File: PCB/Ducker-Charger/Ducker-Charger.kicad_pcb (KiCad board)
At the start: 2 copper layers, 7 parts, among them J1 Conn_01x02, Q1 NCE3080K, Q2 NCE3080K, Q3 NCE3080K, Q4 NCE3080K, U1 IP5389_CN_AACD_WC4QD

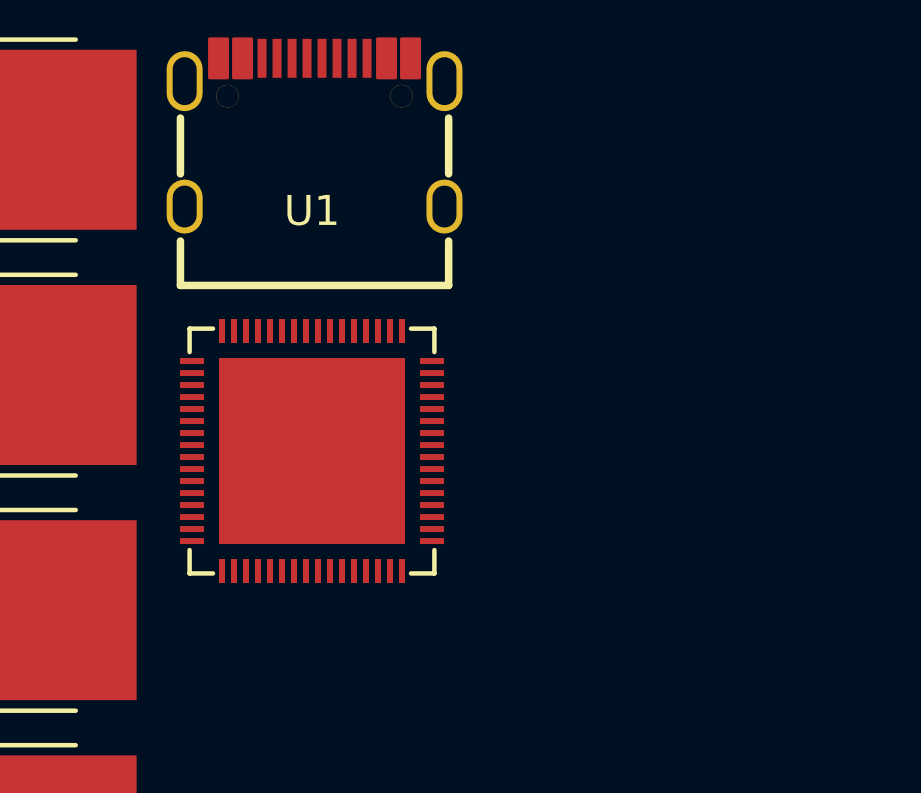
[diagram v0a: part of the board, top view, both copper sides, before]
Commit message: feat: started BMS configuration
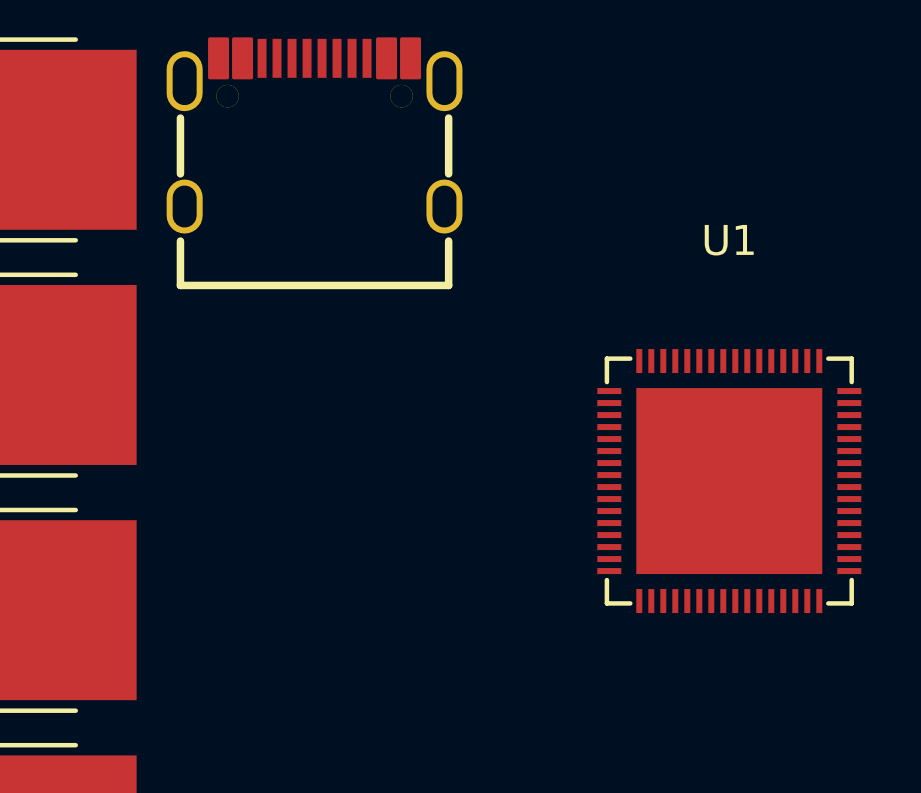
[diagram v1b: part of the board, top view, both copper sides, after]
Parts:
- moved U1 13.9 mm to (270.2, 140.2)
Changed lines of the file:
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@@
 	(footprint "EasyEDA:QFN-64_L8.0-W8.0-P0.40-TL-EP6.2"
 		(layer "F.Cu")
-		(at 256.32 139.16)
+		(at 270.23 140.16)
 		(property "Reference" "U1"
 			(at 0 -8 0)

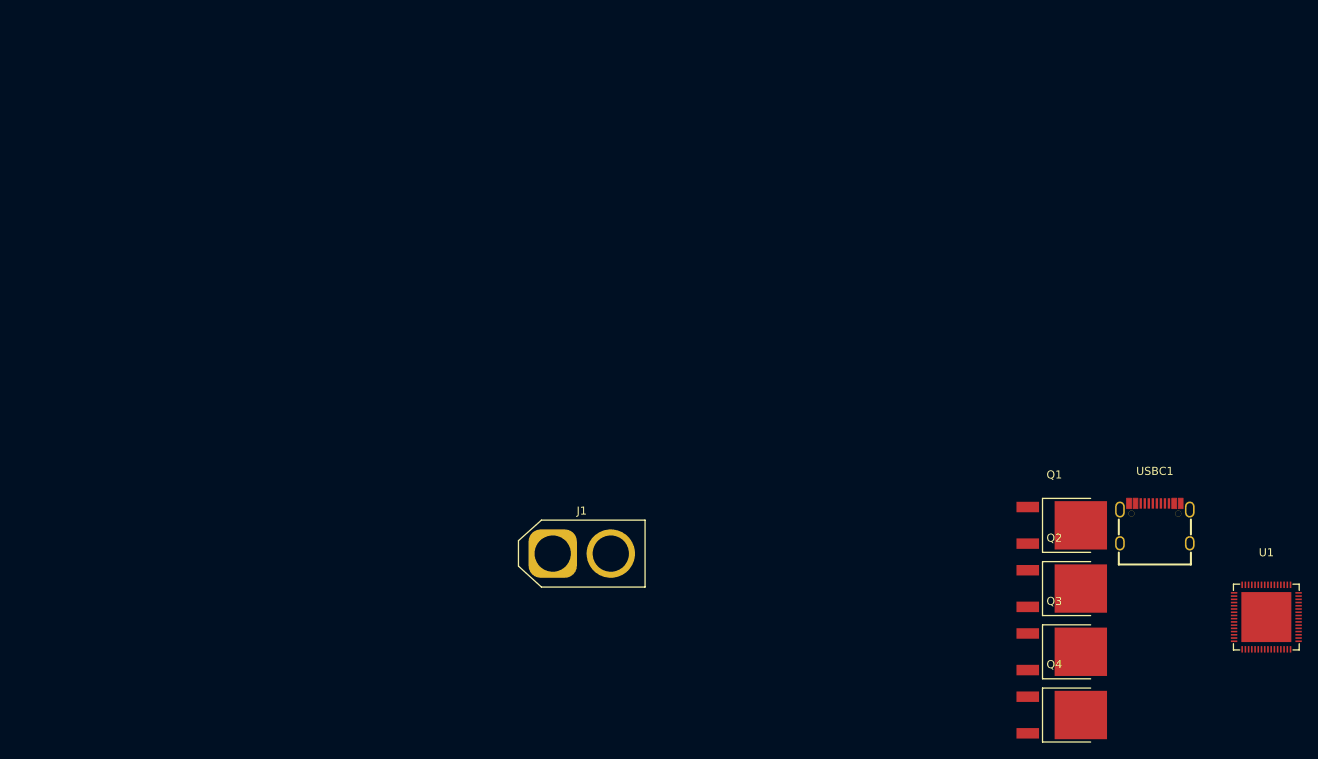
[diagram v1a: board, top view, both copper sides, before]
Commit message: feat: progressed overall schematic
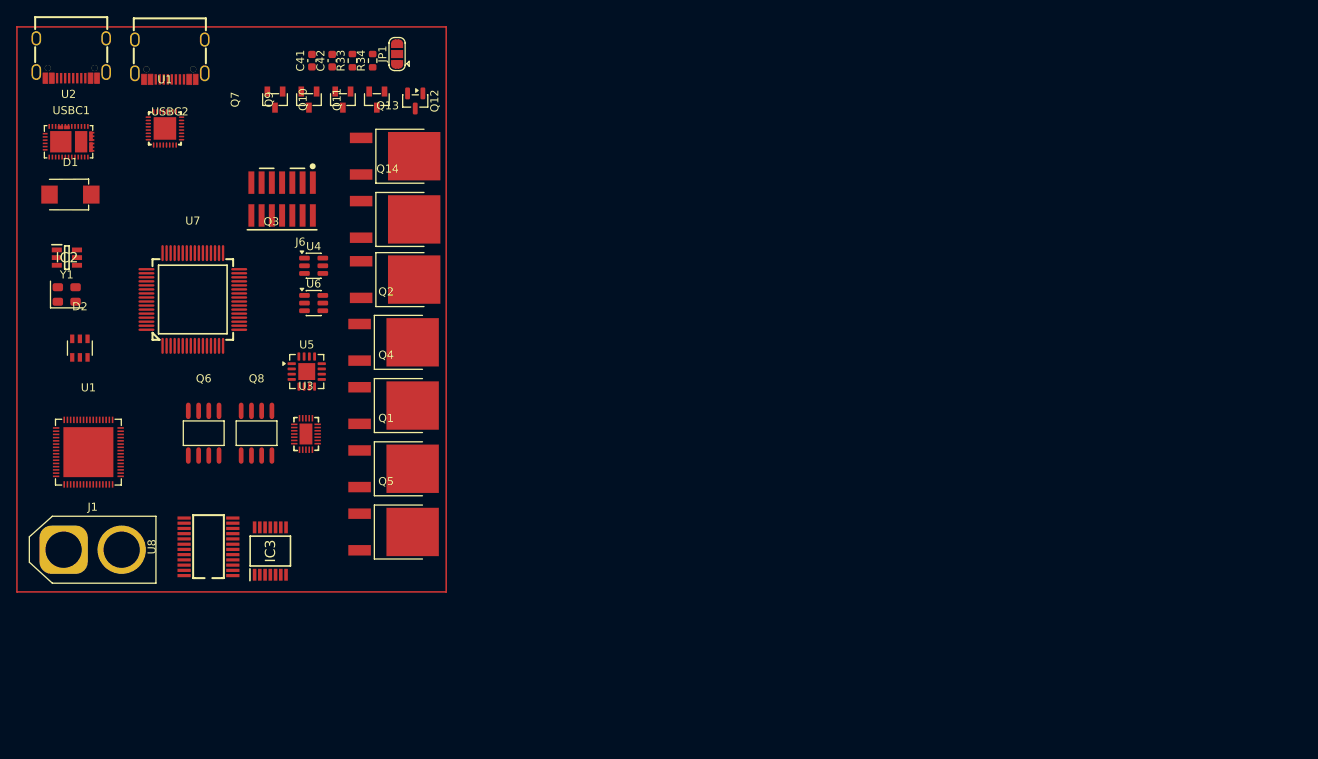
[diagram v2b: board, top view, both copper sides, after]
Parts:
- added C41: 18p, Capacitor_SMD:C_0603_1608Metric, F.Cu at (151.9, 71.2)
- added C42: 18p, Capacitor_SMD:C_0603_1608Metric, F.Cu at (154.4, 71.2)
- added D1: SMBJ22A-E3/52, EasyEDA:SMB_L4.3-W3.6-LS5.4-RD, F.Cu at (121.9, 87.8)
- added D2: USBLC6-4SC6, EasyEDA:SOT-23-6_L2.9-W1.6-P0.95-LS2.8-BL, F.Cu at (123.1, 106.8)
- added IC2: TPS54202HDDCT, TPS54202HDDCT:SOT95P280X110-6N, F.Cu at (121.5, 95.6)
- added IC3: BQ34Z100PWR-R2, BQ34Z100PWR:SOP65P640X120-14N, F.Cu at (146.7, 132.0)
- added J6: Debug, Eagle_Connectors:SAMTEC_FTSH-107-01-L-DV-K-TR, F.Cu at (148.2, 88.3)
- added JP1: Boot, Jumper:SolderJumper-3_P1.3mm_Open_RoundedPad1.0x1.5mm, F.Cu at (162.4, 70.3)
- added Q10: AO3400A, EasyEDA:SOT-23-3_L2.9-W1.3-P1.90-LS2.4-BR, F.Cu at (155.7, 76.0)
- added Q11: AO3400A, EasyEDA:SOT-23-3_L2.9-W1.3-P1.90-LS2.4-BR, F.Cu at (159.9, 76.0)
- added Q12: BC846, Package_TO_SOT_SMD:SOT-23, F.Cu at (164.7, 76.2)
- added Q13: NCE3080K, EasyEDA:TO-252-2_L6.6-W6.1-P4.57-LS9.9-TL-CW, F.Cu at (161.3, 83.0)
- added Q14: NCE3080K, EasyEDA:TO-252-2_L6.6-W6.1-P4.57-LS9.9-TL-CW, F.Cu at (161.3, 90.8)
- added Q3: NCE3080K, EasyEDA:TO-252-2_L6.6-W6.1-P4.57-LS9.9-TL-CW, F.Cu at (161.3, 98.3)
- added Q6: AO4407A, EasyEDA:SOIC-8_L4.9-W3.9-P1.27-LS6.0-BL, F.Cu at (138.5, 117.4)
- added Q7: AO3400A, EasyEDA:SOT-23-3_L2.9-W1.3-P1.90-LS2.4-BR, F.Cu at (147.3, 76.0)
- added Q8: AO4407A, EasyEDA:SOIC-8_L4.9-W3.9-P1.27-LS6.0-BL, F.Cu at (145.0, 117.4)
- added Q9: AO3400A, EasyEDA:SOT-23-3_L2.9-W1.3-P1.90-LS2.4-BR, F.Cu at (151.5, 76.0)
- added R33: 1k, Resistor_SMD:R_0603_1608Metric, F.Cu at (156.9, 71.2)
- added R34: 10k, Resistor_SMD:R_0603_1608Metric, F.Cu at (159.4, 71.2)
- added U1: BQ25713RSNR, EasyEDA:QFN-32_L4.0-W4.0-P0.40-TL-EP2.8, F.Cu at (133.7, 79.6)
- added U2: TPS25750DRJKR, EasyEDA:QFN-38_L6.0-W4.0-P0.40-TL-EP_RJK, F.Cu at (121.7, 81.2)
- added U3: STPD01PUR, EasyEDA:QFN-24_L4.0-W3.0-P0.40-TL-EP, F.Cu at (151.1, 117.5)
- added U4: TPS54302, Package_TO_SOT_SMD:SOT-23-6, F.Cu at (152.1, 96.6)
- added U5: INA3221, Package_DFN_QFN:Texas_RGV0016A_VQFN-16-1EP_4x4mm_P0.65mm_EP2.1x2.1mm, F.Cu at (151.2, 109.7)
- added U6: TPS54302, Package_TO_SOT_SMD:SOT-23-6, F.Cu at (152.1, 101.2)
- added U7: STM32F401RBT6, EasyEDA:LQFP-64_L10.0-W10.0-P0.50-LS12.0-BL, F.Cu at (137.1, 100.8)
- added U8: BQ7791500PWR, EasyEDA:TSSOP-24_L7.8-W4.4-P0.65-LS6.4-BL, F.Cu at (139.1, 131.4)
- added USBC2: TYPE-C-31-M-12, EasyEDA:USB-C_SMD-TYPE-C-31-M-12_1, F.Cu at (134.3, 71.0)
- added Y1: 16MHz, Crystal:Crystal_SMD_EuroQuartz_MT-4Pin_3.2x2.5mm, F.Cu at (121.5, 100.2)
- moved U1 147.5 mm to (124.2, 119.7)
- moved USBC1 146.2 mm to (122.0, 70.9), turned to 180 degrees
- moved Q1 85.9 mm to (161.1, 121.8)
- moved Q2 85.9 mm to (161.1, 106.1)
- moved Q4 85.9 mm to (161.1, 113.9)
- moved Q5 85.9 mm to (161.1, 129.6)
- moved J1 60.7 mm to (121.1, 131.8)
- renumbered Q3 to Q1, Q1 to Q2, Q2 to Q4, Q4 to Q5
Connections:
- Q1 pad 1: unconnected-(Q3-G-Pad1) -> Net-(Q1-G)
- Q1 pad 2: unconnected-(Q3-D-Pad2) -> /High_pow/ACN
- Q1 pad 3: unconnected-(Q3-S-Pad3) -> /High_pow/SW1
- Q2 pad 1: unconnected-(Q1-G-Pad1) -> Net-(Q2-G)
- Q2 pad 2: unconnected-(Q1-D-Pad2) -> /High_pow/V_SYS_A
- Q2 pad 3: unconnected-(Q1-S-Pad3) -> /High_pow/SW2
- Q4 pad 1: unconnected-(Q2-G-Pad1) -> Net-(Q4-G)
- Q4 pad 2: unconnected-(Q2-D-Pad2) -> /High_pow/SW2
- Q4 pad 3: unconnected-(Q2-S-Pad3) -> GND
- Q5 pad 1: unconnected-(Q4-G-Pad1) -> Net-(Q5-G)
- Q5 pad 2: unconnected-(Q4-D-Pad2) -> /High_pow/SW1
- Q5 pad 3: unconnected-(Q4-S-Pad3) -> GND
- USBC1 pad 1: unconnected-(USBC1-EH-Pad1) -> GND
- USBC1 pad 2: unconnected-(USBC1-EH-Pad2) -> GND
- USBC1 pad 3: unconnected-(USBC1-EH-Pad3) -> GND
- USBC1 pad 4: unconnected-(USBC1-EH-Pad4) -> GND
- USBC1 pad A1B12: unconnected-(USBC1-GND-PadA1B12) -> GND
- USBC1 pad A4B9: unconnected-(USBC1-VBUS-PadA4B9) -> /High_pow/ACP
- USBC1 pad A5: unconnected-(USBC1-CC1-PadA5) -> /High_pow/CC1
- USBC1 pad A6: unconnected-(USBC1-DP1-PadA6) -> /High_pow/DP
- USBC1 pad A7: unconnected-(USBC1-DN1-PadA7) -> /High_pow/DN
- USBC1 pad B1A12: unconnected-(USBC1-GND-PadB1A12) -> GND
- USBC1 pad B4A9: unconnected-(USBC1-VBUS-PadB4A9) -> /High_pow/ACP
- USBC1 pad B5: unconnected-(USBC1-CC2-PadB5) -> /High_pow/CC2
- USBC1 pad B6: unconnected-(USBC1-DP2-PadB6) -> /High_pow/DP
- USBC1 pad B7: unconnected-(USBC1-DN2-PadB7) -> /High_pow/DN
